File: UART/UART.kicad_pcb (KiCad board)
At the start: 4 copper layers, 33 x 17.8 mm, 56 parts, among them J1 USB_B_Mini, J2 Conn_01x06, U1 FT232H, U2 93CxxB, U3 AZ1117-3.3, Y1 12MHz

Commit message: moved documentation text
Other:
- board text removed: "TXDEN"

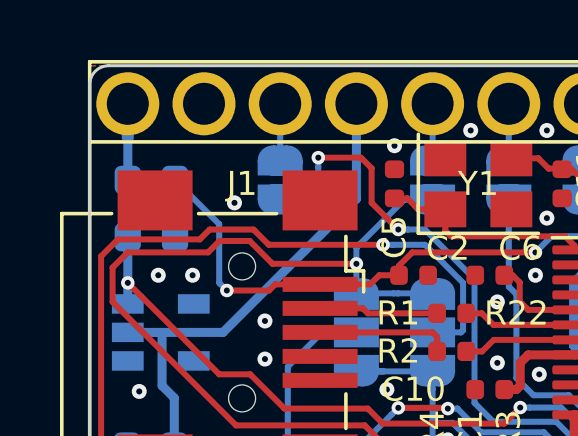
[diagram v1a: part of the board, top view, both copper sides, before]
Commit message: fix some ERC/DRC
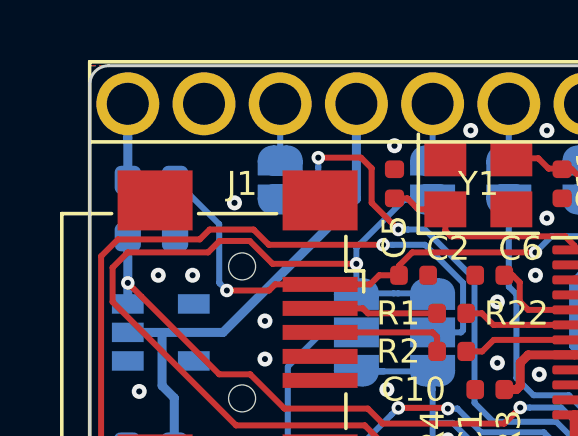
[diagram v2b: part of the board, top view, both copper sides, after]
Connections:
- A1 pad 24: (no net) -> +5V
